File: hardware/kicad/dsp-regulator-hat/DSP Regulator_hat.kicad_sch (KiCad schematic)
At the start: 141 parts, among them J1 Wire con, J10 Wire con, J11 Wire con, J12 Wire con, J2 Wire con, J3 Wire con, J4 Left Side, J5 Conn_01x06_Socket, J6 Right Side, J7 Front Panel, J8 I2C bus, J9 I2C bus, Q1 PSMN5R2-60YL, Q10 PSMN5R2, Q11 PSMN5R2, Q12 PSMN5R2-60YL, Q2 PSMN5R2-60YL, Q3 PSMN5R2-60YL, Q4 PSMN5R2, Q5 PSMN5R2', Q6 PSMN5R2-60YL, Q7 PSMN5R2-60YL, Q8 PSMN5R2-60YL, Q9 PSMN5R2-60YL, U1 INA3221-AIRGVR, U2 INA3221-AIRGVR, U3 INA3221-AIRGVR, U4 74HC595D, U5 74HC595D, U6 W25Q128, U7 ESP32-C6-DevKitM-1

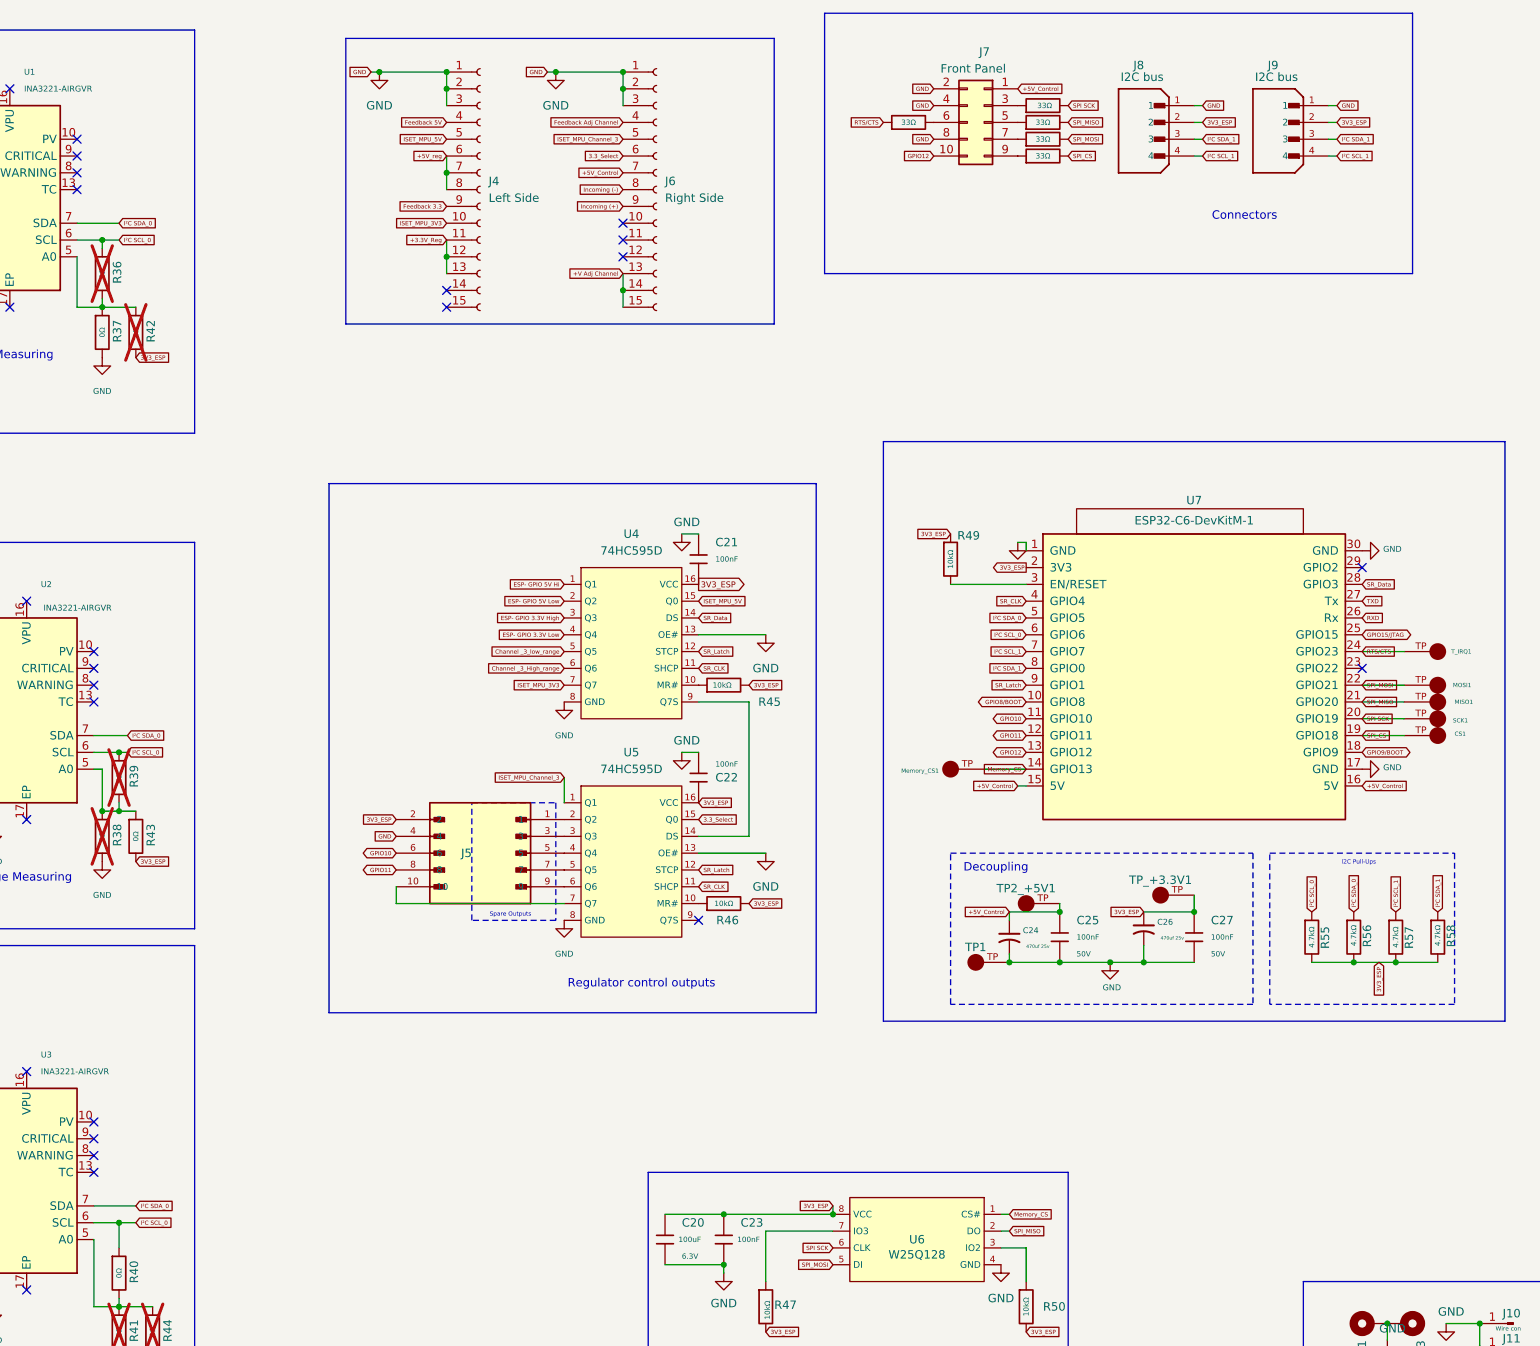
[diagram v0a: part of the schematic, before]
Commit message: Add HatPowerTelemetry class for power telemetry management
- Introduced HatPowerTelemetry class to manage power telemetry for various rails.
- Defined enums for HatRail and HatRange to represent different power rails and measurement ranges.
- Created structures for InaTap, RailMapping, RailMeasurement, and RailCalibration to encapsulate relevant data.
- Implemented methods for setting INA addresses, reading measurements, applying calibration, and managing shunt configurations.
- Added functionality for automatic range switching based on current thresholds.
- Included methods for printing telemetry mapping and calibration data for debugging purposes.
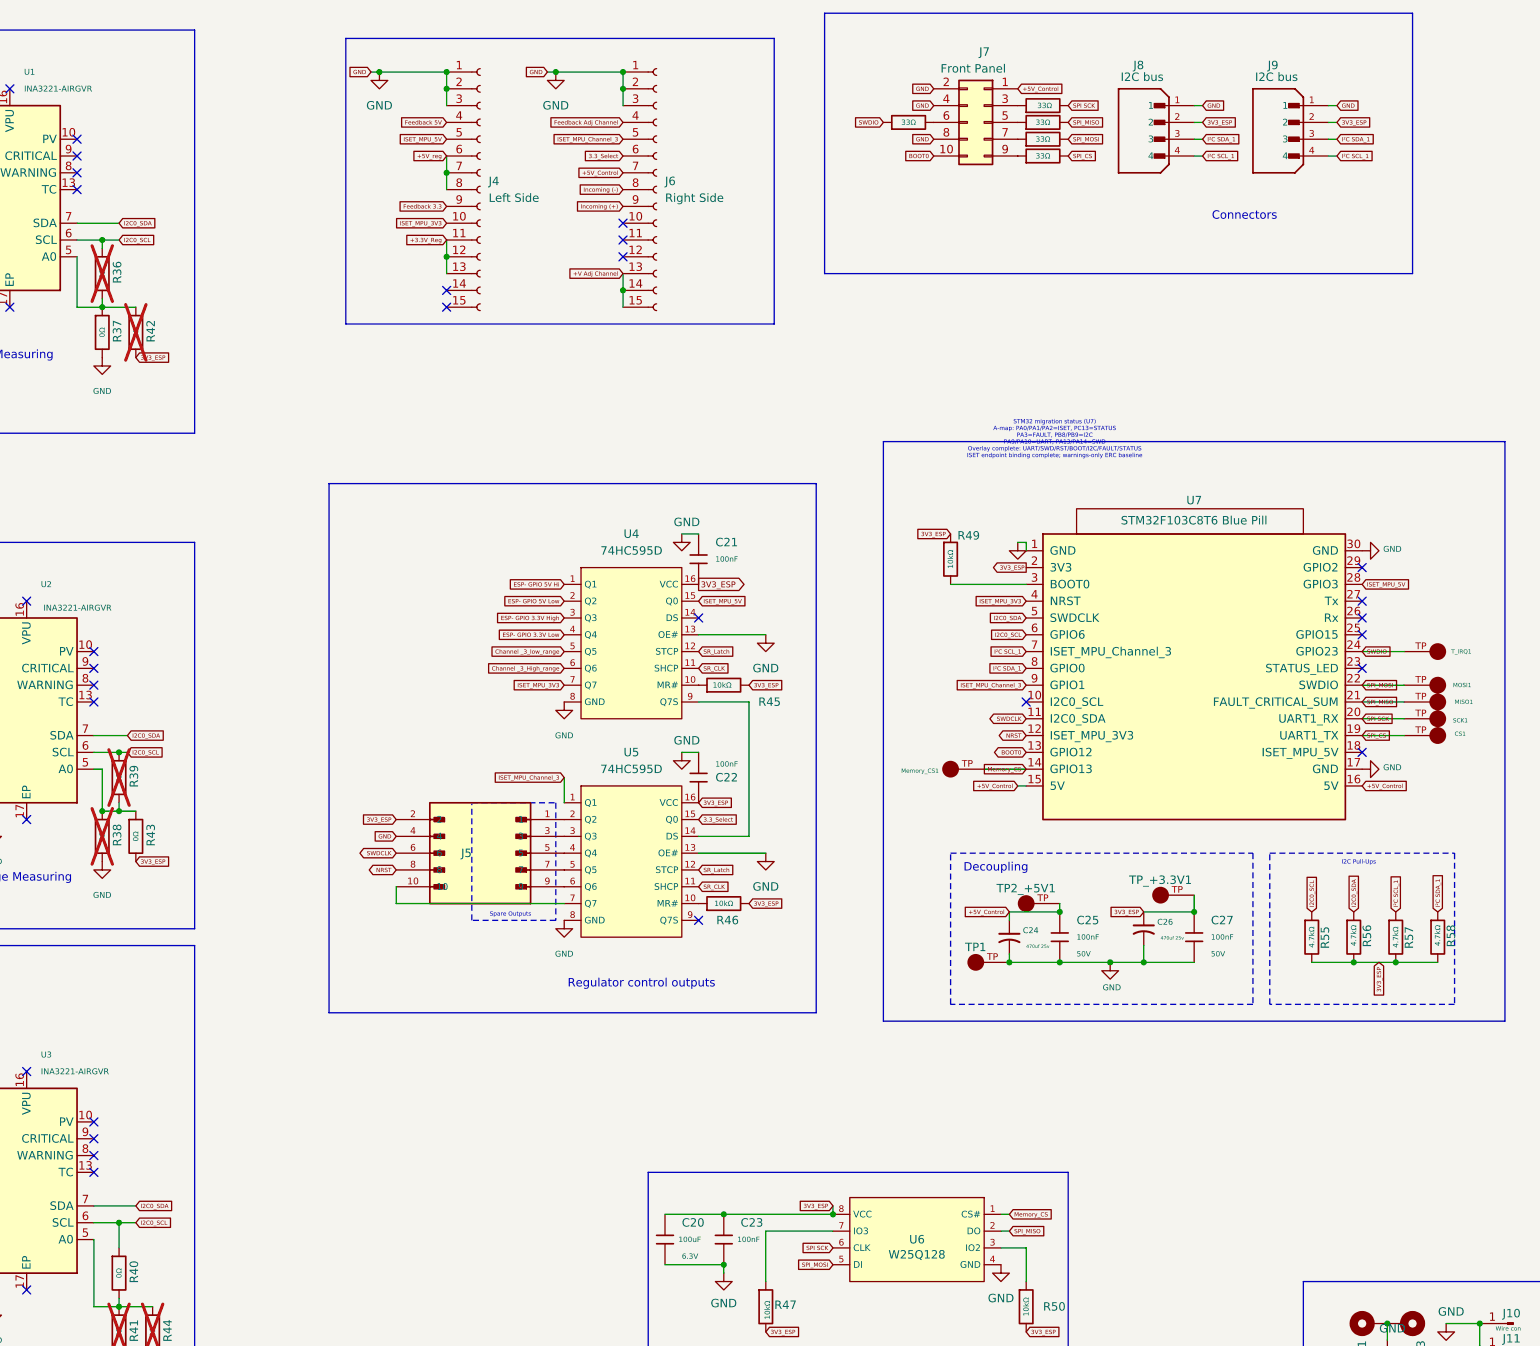
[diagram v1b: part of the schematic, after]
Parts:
- U7: value ESP32-C6-DevKitM-1 -> STM32F103C8T6 Blue Pill; footprint RF_Module:ESP32-C3-DevKitM-1 -> Module:BluePill_STM32F103C8; symbol Espressif:ESP32-C6-DevKitM-1 -> Local:BluePill_STM32F103C8_Migrated; MigrationState (none) -> Label + symbol migration complete; KERC-04 bench evidence p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; MigrationTarget (none) -> STM32F103C8T6 Blue Pill
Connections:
- net ISET_MPU_5V: now also U7.28 (GPIO3)
- net SR_CLK: no longer U7.4 (GPIO4)
- net SR_Latch: no longer U7.9 (GPIO1)
- net  ISET_MPU_3V3 renamed ISET_MPU_3V3
- net ISET_MPU_3V3: now also U7.4 (NRST)
- net  ISET_MPU_Channel_3 renamed ISET_MPU_Channel_3
- net ISET_MPU_Channel_3: now also U7.9 (GPIO1)
- net GPIO10 renamed SWDCLK
- net GPIO11 renamed NRST
- net GPIO12 renamed BOOT0
- net GPIO15/JTAG: no longer names the net of U7.25 (GPIO15)
- net GPIO8/BOOT: no longer names the net of U7.10 (I2C0_SCL)
- net GPIO9/BOOT: no longer names the net of U7.18 (ISET_MPU_5V)
- net I²C SCL_0 renamed I2C0_SCL
- net I²C SDA_0 renamed I2C0_SDA
- net RTS/CTS renamed SWDIO
- net RXD: no longer names the net of U7.26 (Rx)
- net SR_Data: no longer names the net of U4.14 (DS)
- net SR_Data: no longer U7.28 (GPIO3)
- net TXD: no longer names the net of U7.27 (Tx)
- no-connect marks 30 -> 36
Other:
- note added: "STM32 migration status (U7) A-map: PA0/PA1/PA2=ISET, PC13=STATUS PA3=FAULT, PB8/PB9=I2C PA9/PA10=UART, PA13/PA14=SWD Overlay complete: UART/SWD/RST/BOOT/I2C/FAULT/STATUS ISET endpoint binding complete; warnings-only ERC baseline"
